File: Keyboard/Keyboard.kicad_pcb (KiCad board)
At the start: 4 copper layers, 327 x 135 mm, 177 parts, among them J1 Conn_01x06, J2 Conn_01x04, J3 Conn_01x16

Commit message: Finished First Pass of Schematic and Layout
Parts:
- removed J1: Conn_01x06, Connector_PinHeader_2.54mm:PinHeader_1x06_P2.54mm_Vertical
- removed J3: Conn_01x16, Connector_PinHeader_2.54mm:PinHeader_1x16_P2.54mm_Vertical
- added J4: Conn_02x20_Odd_Even, Keyboard:SAMTEC_ERF8-020-05.0-L-DV-K-TR, B.Cu at (139.9, 109.6)
- added R1: 10k, Resistor_SMD:R_0805_2012Metric_Pad1.20x1.40mm_HandSolder, B.Cu at (448.0, 111.7)
- added R10: 10k, Resistor_SMD:R_0805_2012Metric_Pad1.20x1.40mm_HandSolder, B.Cu at (447.7, 187.9)
- added R11: 10k, Resistor_SMD:R_0805_2012Metric_Pad1.20x1.40mm_HandSolder, B.Cu at (447.7, 209.2)
- added R12: 10k, Resistor_SMD:R_0805_2012Metric_Pad1.20x1.40mm_HandSolder, B.Cu at (447.7, 206.9)
- added R13: 10k, Resistor_SMD:R_0805_2012Metric_Pad1.20x1.40mm_HandSolder, B.Cu at (449.0, 102.0)
- added R2: 10k, Resistor_SMD:R_0805_2012Metric_Pad1.20x1.40mm_HandSolder, B.Cu at (448.0, 113.9)
- added R3: 10k, Resistor_SMD:R_0805_2012Metric_Pad1.20x1.40mm_HandSolder, B.Cu at (447.7, 133.0)
- added R4: 10k, Resistor_SMD:R_0805_2012Metric_Pad1.20x1.40mm_HandSolder, B.Cu at (447.7, 130.7)
- added R5: 10k, Resistor_SMD:R_0805_2012Metric_Pad1.20x1.40mm_HandSolder, B.Cu at (447.7, 152.0)
- added R6: 10k, Resistor_SMD:R_0805_2012Metric_Pad1.20x1.40mm_HandSolder, B.Cu at (447.8, 149.8)
- added R7: 10k, Resistor_SMD:R_0805_2012Metric_Pad1.20x1.40mm_HandSolder, B.Cu at (447.7, 171.1)
- added R8: 10k, Resistor_SMD:R_0805_2012Metric_Pad1.20x1.40mm_HandSolder, B.Cu at (447.7, 168.8)
- added R9: 10k, Resistor_SMD:R_0805_2012Metric_Pad1.20x1.40mm_HandSolder, B.Cu at (447.7, 190.1)
- added S1: PEC12R-4220F-S0024, Keyboard:XDCR_PEC12R-4220F-S0024, F.Cu at (459.0, 89.0)
- D1, D10, D11, D12, D13, D14, D15, D16, D17, D18, D19, D2, D20, D21, D22, D23, D24, D25, D26, D27, D28, D29, D3, D30, D31, D32, D33, D34, D35, D36, D37, D38, D39, D4, D40, D41, D42, D43, D44, D45, D46, D47, D48, D49, D5, D50, D51, D52, D53, D54, D55, D56, D57, D58, D59, D6, D60, D61, D62, D63, D64, D65, D66, D67, D68, D69, D7, D70, D71, D72, D73, D74, D75, D76, D77, D78, D79, D8, D80, D81, D82, D83, D84, D9: footprint Diode_SMD:D_0805_2012Metric -> Diode_SMD:D_0805_2012Metric_Pad1.15x1.40mm_HandSolder
- moved H1 279.9 mm to (246.0, 203.0)
- moved H6 264.7 mm to (454.0, 121.0)
- moved J2 224.0 mm to (140.1, 123.6)
- moved H5 215.7 mm to (302.6, 203.0)
- moved H3 207.3 mm to (137.0, 139.4)
- moved H2 206.8 mm to (454.3, 196.3)
- moved D12 132.2 mm to (372.2, 106.0)
- moved D13 132.2 mm to (391.2, 106.0)
- moved D16 132.2 mm to (448.4, 106.0)
- moved D23 132.2 mm to (276.9, 125.0)
- moved D24 132.2 mm to (296.0, 125.0)
- moved D28 132.2 mm to (372.2, 125.0)
- moved D29 132.2 mm to (391.2, 125.0)
- moved D30 132.2 mm to (419.8, 125.0)
- moved D31 132.2 mm to (448.4, 125.0)
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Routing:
- net ENC_SW: track 0.00 -> 346.2 mm, vias 0 -> 2
- net ENC_B: track 0.00 -> 328.8 mm, vias 0 -> 2
- net ENC_A: track 0.00 -> 323.2 mm, vias 0 -> 2
- net COL9: track 90.8 -> 302.7 mm, vias 0 -> 1
- net COL15: track 238.7 -> 438.2 mm, vias 0 -> 1
- net COL14: track 223.6 -> 417.8 mm, vias 0 -> 1
- net COL13: track 216.6 -> 405.9 mm, vias 0 -> 1
- net COL12: track 219.9 -> 406.2 mm, vias 0 -> 1
- net COL11: track 186.5 -> 367.6 mm, vias 0 -> 1
- net COL10: track 167.9 -> 345.5 mm, vias 0 -> 1
- net COL6: track 90.4 -> 252.2 mm
- net COL7: track 138.2 -> 297.4 mm
- net COL8: track 127.3 -> 272.3 mm, vias 0 -> 1
- net ROW3: track 460.4 -> 560.2 mm
- net ROW4: track 475.8 -> 573.6 mm
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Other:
- board size 327 x 135 mm -> 340 x 140 mm
- board text removed: "Row0"
- board text removed: "Row5"

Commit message: First rev of keyboard main board complete, starting on controller board next
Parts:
- moved H1 119.6 mm to (279.0, 88.0)
- moved H3 54.6 mm to (155.3, 88.0)
- moved H6 46.0 mm to (422.0, 88.0)
- moved S1 18.0 mm to (441.0, 90.0), turned to -90 degrees
- moved R13 12.6 mm to (445.0, 90.0)
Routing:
- net ENC_SW: track 346.2 -> 318.4 mm
- net ENC_B: track 328.8 -> 302.1 mm
- net COL3: track 205.4 -> 184.3 mm
- net ENC_A: track 323.2 -> 303.5 mm
- net VCC: track 19.5 -> 21.5 mm, vias 10 -> 11
- added copper zone on In1.Cu, net GND
- added copper zone on In2.Cu, net VCC
- removed copper zone on In2.Cu, net GND
- removed copper zone on In1.Cu, net VCC
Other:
- board size 340 x 140 mm -> 330 x 137 mm

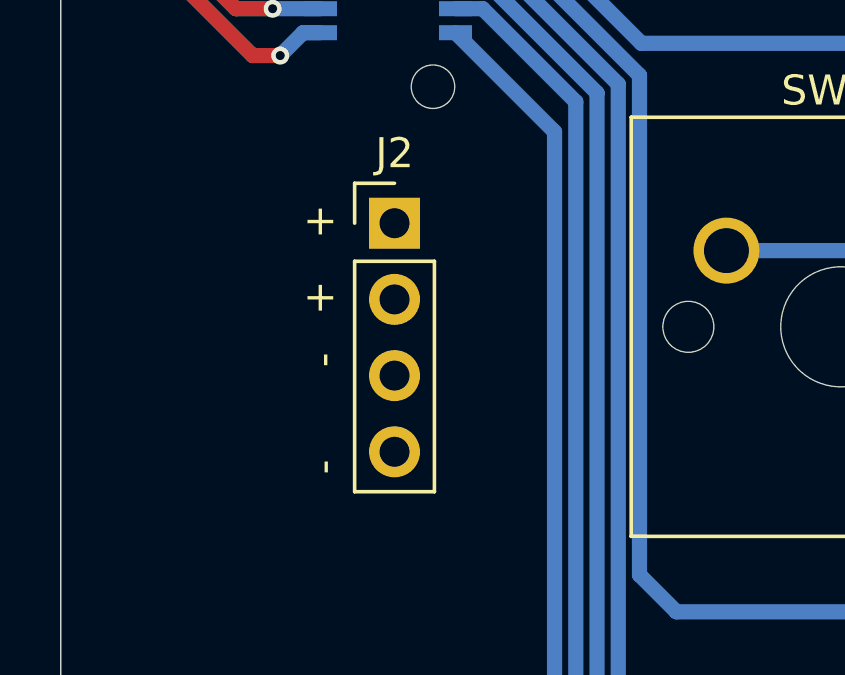
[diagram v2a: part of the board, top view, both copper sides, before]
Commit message: Finished First Rev Of Both PCB's, after testing fits in freecad, will  move onto ordrering board
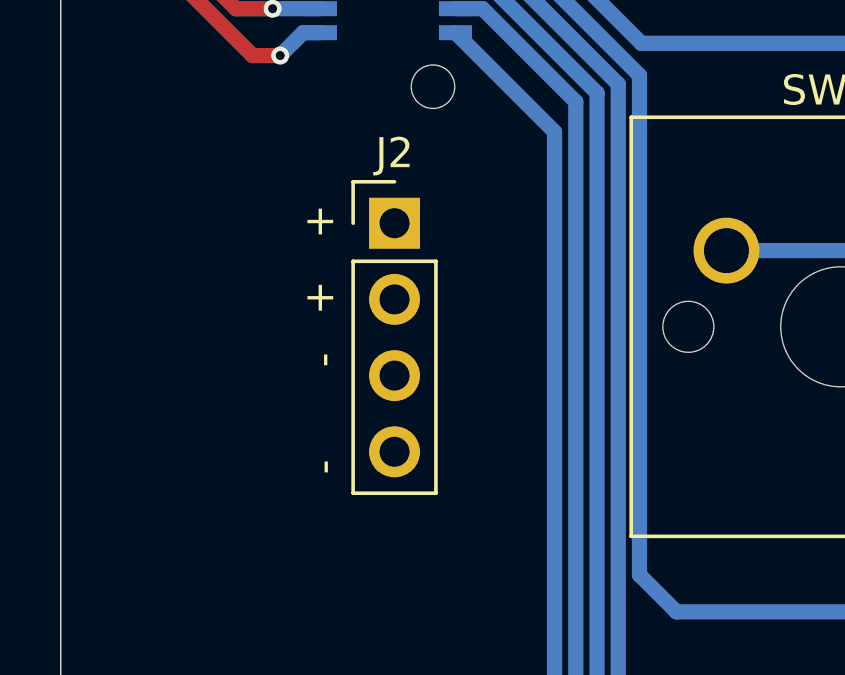
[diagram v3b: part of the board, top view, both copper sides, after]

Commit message: Last Commit Before JLC Order, Looking to do BOM next
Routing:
- added copper zone on In2.Cu, net GND
- added copper zone on In1.Cu, net VCC
- removed copper zone on In1.Cu, net GND
- removed copper zone on In2.Cu, net VCC
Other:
- board size 330 x 137 mm -> 333 x 135.5 mm
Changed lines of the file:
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@@
 			(outputformat 1)
 			(mirror no)
-			(drillshape 1)
+			(drillshape 0)
 			(scaleselection 1)
-			(outputdirectory "")
+			(outputdirectory "Gerber/")
 		)
 	)
@@
 	)
 	(gr_line
-		(start 444 82)
-		(end 129 82)
+		(start 461 208.5)
+		(end 110.5 208.5)
 		(stroke
 			(width 0.1)
@@
 	)
 	(gr_line
-		(start 459 206)
-		(end 459 82)
+		(start 136 81.5)
+		(end 453 81.5)
 		(stroke
-			(width 0.1)
+			(width 0.05)
 			(type default)
 		)
-		(layer "Dwgs.User")
+		(layer "Edge.Cuts")
 	)
 	(gr_line
-		(start 129 91)
-		(end 138 82)
+		(start 135.994796 81.504478)
+		(end 136 81.5)
 		(stroke
-			(width 0.1)
+			(width 0.05)
 			(type default)
 		)
-		(layer "Dwgs.User")
+		(layer "Edge.Cuts")
 	)
 	(gr_line
-		(start 129 205)
-		(end 143 219)
+		(start 461 208.5)
+		(end 461 89.5)
 		(stroke
-			(width 0.1)
+			(width 0.05)
 			(type default)
 		)
-		(layer "Dwgs.User")
+		(layer "Edge.Cuts")
 	)
-	(gr_line
-		(start 129 82)
-		(end 129 219)
+	(gr_arc
+		(start 136.5052 216.99407)
+		(mid 130.494796 214.504478)
+		(end 128.005204 208.494821)
 		(stroke
-			(width 0.1)
+			(width 0.05)
 			(type default)
 		)
-		(layer "Dwgs.User")
+		(layer "Edge.Cuts")
 	)
-	(gr_line
-		(start 450 82)
-		(end 459 91)
+	(gr_arc
+		(start 127.994796 89.5052)
+		(mid 130.337942 83.847624)
+		(end 135.994796 81.504478)
 		(stroke
-			(width 0.1)
+			(width 0.05)
 			(type default)
 		)
-		(layer "Dwgs.User")
+		(layer "Edge.Cuts")
 	)
 	(gr_line
-		(start 459 82)
-		(end 444 82)
+		(start 128.005204 208.494821)
+		(end 127.994796 89.5052)
 		(stroke
-			(width 0.1)
+			(width 0.05)
 			(type default)
 		)
-		(layer "Dwgs.User")
+		(layer "Edge.Cuts")
 	)
-	(gr_line
-		(start 445 219)
-		(end 459 205)
+	(gr_arc
+		(start 453 81.5)
+		(mid 458.656854 83.843146)
+		(end 461 89.5)
 		(stroke
-			(width 0.1)
+			(width 0.05)
 			(type default)
 		)
-		(layer "Dwgs.User")
+		(layer "Edge.Cuts")
 	)
-	(gr_line
-		(start 129 219)
-		(end 459 219)
+	(gr_arc
+		(start 461 208.5)
+		(mid 458.510408 214.510408)
+		(end 452.5 217)
 		(stroke
-			(width 0.1)
+			(width 0.05)
 			(type default)
 		)
-		(layer "Dwgs.User")
+		(layer "Edge.Cuts")
 	)
-	(gr_poly
-		(pts
-			(xy 129 91) (xy 138 82) (xy 450 82) (xy 459 91) (xy 459 205) (xy 445 219) (xy 143 219) (xy 129 205)
+	(gr_line
+		(start 136.5052 216.99407)
+		(end 136.5052 217)
+		(stroke
+			(width 0.05)
+			(type default)
 		)
+		(layer "Edge.Cuts")
+	)
+	(gr_line
+		(start 136.5052 217)
+		(end 452.5 217)
 		(stroke
 			(width 0.05)
-			(type solid)
+			(type default)
 		)
-		(fill no)
 		(layer "Edge.Cuts")
 	)
@@
 	)
 	(zone
-		(net 108)
-		(net_name "GND")
+		(net 107)
+		(net_name "VCC")
 		(layer "In1.Cu")
 		(hatch edge 0.5)
@@
 		(polygon
 			(pts
-				(xy 129 91) (xy 138 82) (xy 450 82) (xy 459 91) (xy 459 205) (xy 445 219) (xy 143 219) (xy 129 205)
+				(xy 128 81.5) (xy 461 81.5) (xy 461 217) (xy 128 217)
 			)
 		)
 	)
 	(zone
-		(net 107)
-		(net_name "VCC")
+		(net 108)
+		(net_name "GND")
 		(layer "In2.Cu")
 		(hatch edge 0.5)
-		(priority 1)
 		(connect_pads
 			(clearance 0.5)
@@
 		(polygon
 			(pts
-				(xy 129 91) (xy 138 82) (xy 450 82) (xy 459 91) (xy 459 205) (xy 445 219) (xy 143 219) (xy 129 205)
+				(xy 128 81.5) (xy 461 81.5) (xy 461 217) (xy 128 217)
 			)
 		)
